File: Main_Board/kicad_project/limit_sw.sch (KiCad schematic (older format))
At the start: 70 parts

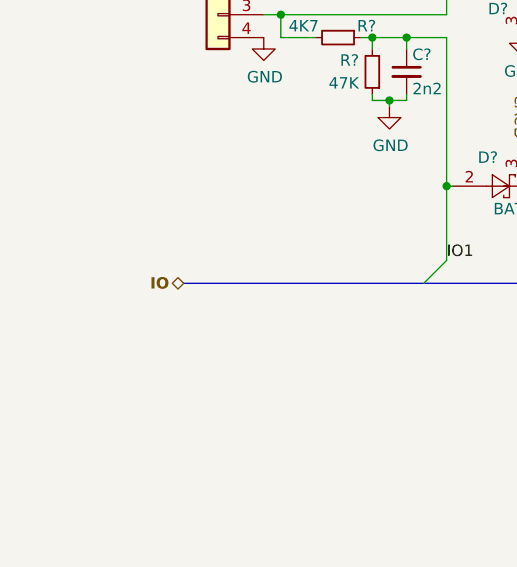
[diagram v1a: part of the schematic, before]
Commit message: fix bus connection
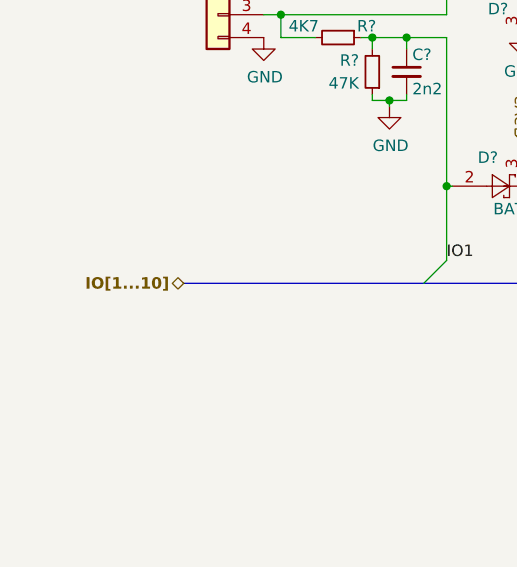
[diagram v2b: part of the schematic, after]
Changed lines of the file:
@@
 $EndComp
 Text HLabel 1550 3925 0    50   BiDi ~ 10
-IO
+IO[1...10]
 Entry Wire Line
 	2700 3825 2600 3925

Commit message: schematic rev1 finished
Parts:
- gave numbers to parts that had none: 70

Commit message: main board: layout start, steppers done
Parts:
- J14, J15, J16, J17, J18, J19, J20, J21, J22, J23: footprint Connector_PinHeader_2.54mm:PinHeader_1x04_P2.54mm_Vertical -> LoaDy:Molex_70543-0003
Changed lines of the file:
@@
 F 0 "J14" H 1700 2925 50  0000 C CNN
 F 1 "IO1" H 1700 2850 50  0000 C CNN
-F 2 "Connector_PinHeader_2.54mm:PinHeader_1x04_P2.54mm_Vertical" H 1700 2650 50  0001 C CNN
+F 2 "LoaDy:Molex_70543-0003" H 1700 2650 50  0001 C CNN
 F 3 "~" H 1700 2650 50  0001 C CNN
 	1    1700 2650
@@
 F 0 "J16" H 4350 2925 50  0000 C CNN
 F 1 "IO2" H 4350 2850 50  0000 C CNN
-F 2 "Connector_PinHeader_2.54mm:PinHeader_1x04_P2.54mm_Vertical" H 4350 2650 50  0001 C CNN
+F 2 "LoaDy:Molex_70543-0003" H 4350 2650 50  0001 C CNN
 F 3 "~" H 4350 2650 50  0001 C CNN
 	1    4350 2650
@@
 F 0 "J20" H 7350 2925 50  0000 C CNN
 F 1 "IO4" H 7350 2850 50  0000 C CNN
-F 2 "Connector_PinHeader_2.54mm:PinHeader_1x04_P2.54mm_Vertical" H 7350 2650 50  0001 C CNN
+F 2 "LoaDy:Molex_70543-0003" H 7350 2650 50  0001 C CNN
 F 3 "~" H 7350 2650 50  0001 C CNN
 	1    7350 2650
@@
 F 0 "J17" H 4700 2925 50  0000 C CNN
 F 1 "IO3" H 4700 2850 50  0000 C CNN
-F 2 "Connector_PinHeader_2.54mm:PinHeader_1x04_P2.54mm_Vertical" H 4700 2650 50  0001 C CNN
+F 2 "LoaDy:Molex_70543-0003" H 4700 2650 50  0001 C CNN
 F 3 "~" H 4700 2650 50  0001 C CNN
 	1    4700 2650
@@
 F 0 "J23" H 10350 2925 50  0000 C CNN
 F 1 "IO6" H 10350 2850 50  0000 C CNN
-F 2 "Connector_PinHeader_2.54mm:PinHeader_1x04_P2.54mm_Vertical" H 10350 2650 50  0001 C CNN
+F 2 "LoaDy:Molex_70543-0003" H 10350 2650 50  0001 C CNN
 F 3 "~" H 10350 2650 50  0001 C CNN
 	1    10350 2650
@@
 F 0 "J21" H 7700 2925 50  0000 C CNN
 F 1 "IO5" H 7700 2850 50  0000 C CNN
-F 2 "Connector_PinHeader_2.54mm:PinHeader_1x04_P2.54mm_Vertical" H 7700 2650 50  0001 C CNN
+F 2 "LoaDy:Molex_70543-0003" H 7700 2650 50  0001 C CNN
 F 3 "~" H 7700 2650 50  0001 C CNN
 	1    7700 2650
@@
 F 0 "J15" H 3175 5125 50  0000 C CNN
 F 1 "IO7" H 3175 5050 50  0000 C CNN
-F 2 "Connector_PinHeader_2.54mm:PinHeader_1x04_P2.54mm_Vertical" H 3175 4850 50  0001 C CNN
+F 2 "LoaDy:Molex_70543-0003" H 3175 4850 50  0001 C CNN
 F 3 "~" H 3175 4850 50  0001 C CNN
 	1    3175 4850
@@
 F 0 "J18" H 5825 5125 50  0000 C CNN
 F 1 "IO8" H 5825 5050 50  0000 C CNN
-F 2 "Connector_PinHeader_2.54mm:PinHeader_1x04_P2.54mm_Vertical" H 5825 4850 50  0001 C CNN
+F 2 "LoaDy:Molex_70543-0003" H 5825 4850 50  0001 C CNN
 F 3 "~" H 5825 4850 50  0001 C CNN
 	1    5825 4850
@@
 F 0 "J19" H 6175 5125 50  0000 C CNN
 F 1 "IO9" H 6175 5050 50  0000 C CNN
-F 2 "Connector_PinHeader_2.54mm:PinHeader_1x04_P2.54mm_Vertical" H 6175 4850 50  0001 C CNN
+F 2 "LoaDy:Molex_70543-0003" H 6175 4850 50  0001 C CNN
 F 3 "~" H 6175 4850 50  0001 C CNN
 	1    6175 4850
@@
 F 0 "J22" H 8825 5125 50  0000 C CNN
 F 1 "IO10" H 8825 5050 50  0000 C CNN
-F 2 "Connector_PinHeader_2.54mm:PinHeader_1x04_P2.54mm_Vertical" H 8825 4850 50  0001 C CNN
+F 2 "LoaDy:Molex_70543-0003" H 8825 4850 50  0001 C CNN
 F 3 "~" H 8825 4850 50  0001 C CNN
 	1    8825 4850
